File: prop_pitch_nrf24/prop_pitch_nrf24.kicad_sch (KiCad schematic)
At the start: 53 parts, among them J1 LOAD1, J2 LOAD2, J3 AVR-UPDI-6, J4 SERVO2, J5 SERVO1, Q1 MMSS8550, U1 ATtiny1616-M, U1 TPS563208DDCR, U2 HX711, U4 AZ1117-5.0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

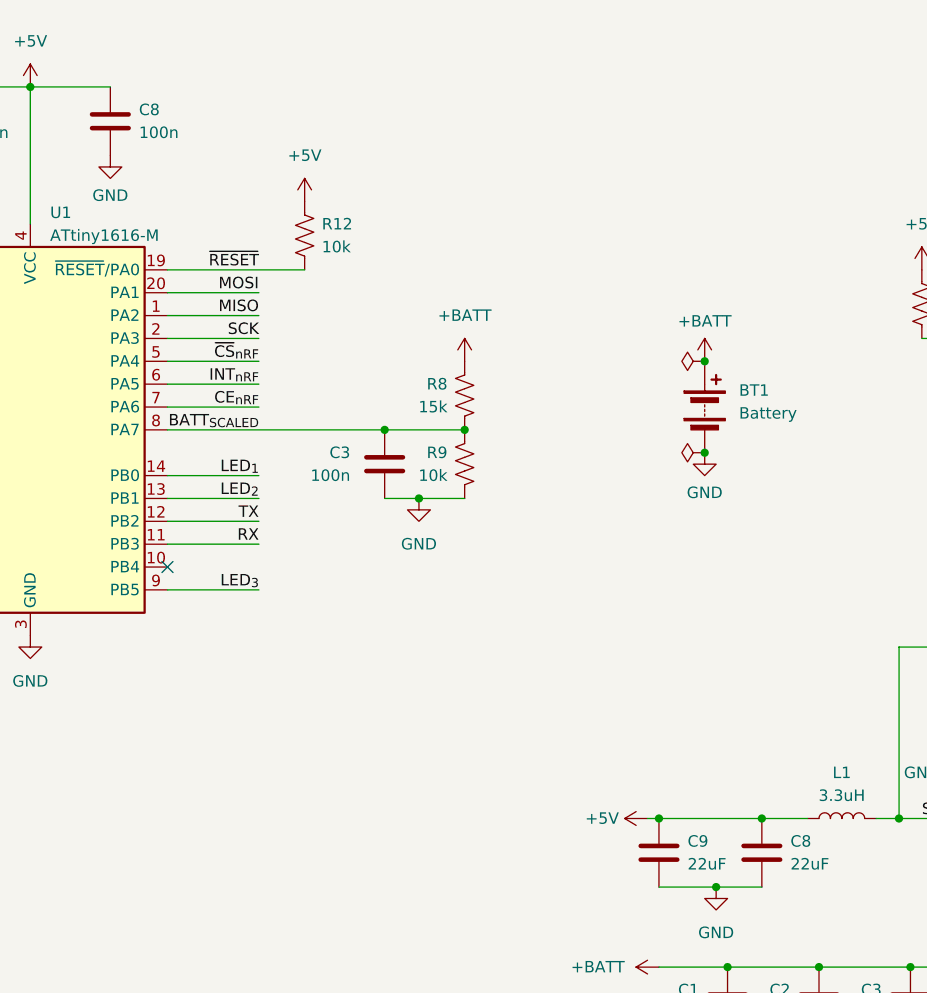
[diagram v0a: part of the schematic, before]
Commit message: Added serial header and address jumper
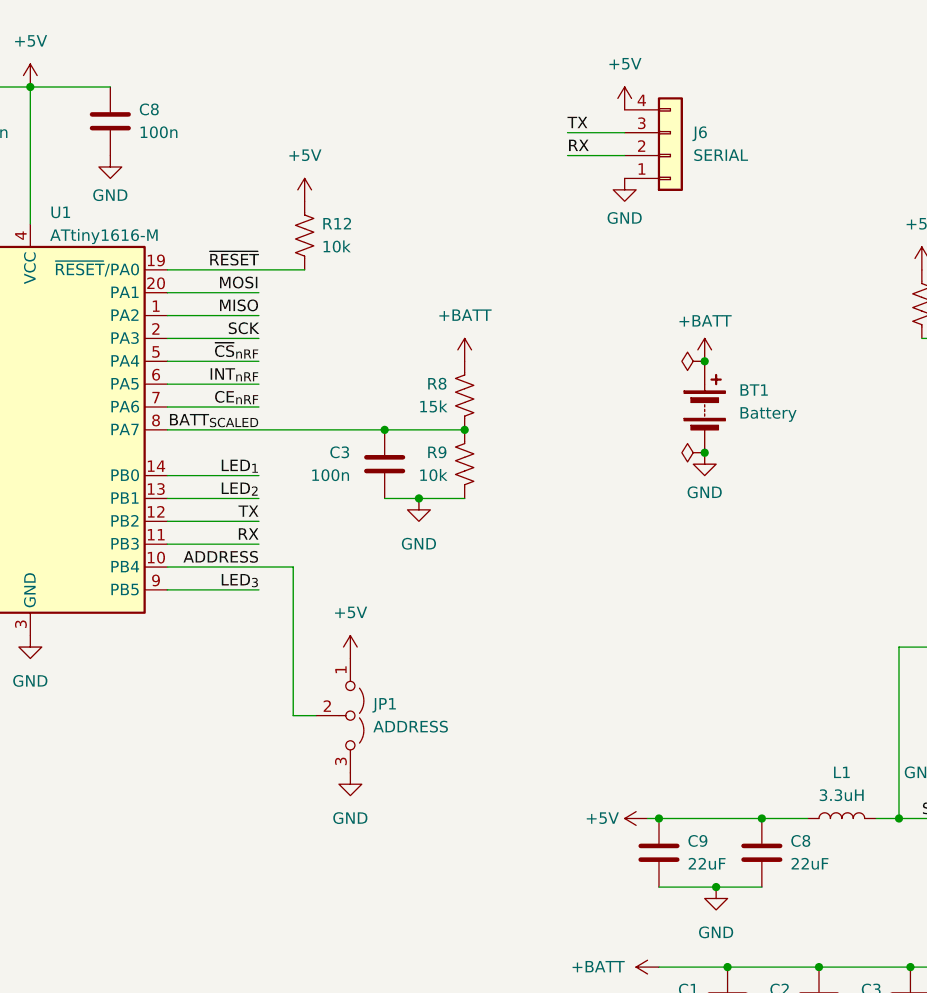
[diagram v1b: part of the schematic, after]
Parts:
- added J6: SERIAL, Connector_PinHeader_2.54mm:PinHeader_1x04_P2.54mm_Vertical, symbol Connector_Generic:Conn_01x04
- added JP1: ADDRESS, Jumper:SolderJumper-3_P1.3mm_Open_Pad1.0x1.5mm_NumberLabels, symbol Jumper:Jumper_3_Open
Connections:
- net +5V: now also J6.4 (Pin_4), JP1.1 (A)
- net GND: now also J6.1 (Pin_1), JP1.3 (B)
- net RX: now also J6.2 (Pin_2)
- net TX: now also J6.3 (Pin_3)
- net ADDRESS: now reaches U1.10 (PB4)
- net ADDRESS: now also JP1.2 (C)
- no-connect marks 2 -> 1
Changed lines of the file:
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@@
   (junction (at 229.87 171.45) (diameter 0) (color 0 0 0 0)
   )
-  (no_connect (at 121.92 76.2))
   (no_connect (at 148.59 153.67))
   (wire (pts (xy 121.92 48.26) (xy 132.08 48.26))
@@
     (stroke (width 0) (type default))
   )
+  (wire (pts (xy 121.92 76.2) (xy 135.89 76.2))
+    (stroke (width 0) (type default))
+  )
   (wire (pts (xy 133.35 133.35) (xy 135.89 133.35))
     (stroke (width 0) (type default))
@@
     (stroke (width 0) (type default))
   )
+  (wire (pts (xy 135.89 76.2) (xy 135.89 92.71))
+    (stroke (width 0) (type default))
+  )
   (wire (pts (xy 121.92 71.12) (xy 132.08 71.12))
     (stroke (width 0) (type default))
@@
     (stroke (width 0) (type default))
   )
+  (wire (pts (xy 172.72 30.48) (xy 166.37 30.48))
+    (stroke (width 0) (type default))
+  )
   (wire (pts (xy 27.94 115.57) (xy 35.56 115.57))
     (stroke (width 0) (type default))
@@
     (stroke (width 0) (type default))
   )
+  (wire (pts (xy 172.72 27.94) (xy 166.37 27.94))
+    (stroke (width 0) (type default))
+  )
   (wire (pts (xy 228.6 99.06) (xy 227.33 99.06))
     (stroke (width 0) (type default))
@@
     (stroke (width 0) (type default))
   )
+  (wire (pts (xy 135.89 92.71) (xy 138.43 92.71))
+    (stroke (width 0) (type default))
+  )
   (wire (pts (xy 40.64 162.56) (xy 50.8 162.56))
     (stroke (width 0) (type default))
@@
     (effects (font (size 1.27 1.27)) (justify left bottom))
   )
+  (label "ADDRESS" (at 132.08 76.2 180) (fields_autoplaced)
+    (effects (font (size 1.27 1.27)) (justify right bottom))
+  )
   (label "SCK" (at 214.63 48.26 0) (fields_autoplaced)
     (effects (font (size 1.27 1.27)) (justify left bottom))
@@
     (effects (font (size 1.27 1.27)) (justify right bottom))
   )
+  (label "TX" (at 166.37 27.94 0) (fields_autoplaced)
+    (effects (font (size 1.27 1.27)) (justify left bottom))
+  )
+  (label "RX" (at 166.37 30.48 0) (fields_autoplaced)
+    (effects (font (size 1.27 1.27)) (justify left bottom))
+  )
   (label "LED_{2}" (at 38.1 66.04 270) (fields_autoplaced)
     (effects (font (size 1.27 1.27)) (justify right bottom))
@@
     )
   )
+  (symbol (lib_id "power:GND") (at 172.72 33.02 0) (unit 1)
+    (in_bom yes) (on_board yes) (dnp no) (fields_autoplaced)
+    (property "Reference" "#PWR049" (at 172.72 39.37 0)
+      (effects (font (size 1.27 1.27)) hide)
+    )
+    (property "Value" "GND" (at 172.72 37.465 0)
+      (effects (font (size 1.27 1.27)))
+    )
+    (property "Footprint" "" (at 172.72 33.02 0)
+      (effects (font (size 1.27 1.27)) hide)
+    )
+    (property "Datasheet" "" (at 172.72 33.02 0)
+      (effects (font (size 1.27 1.27)) hide)
+    )
+    (pin "1")
+    (instances
+      (project "prop_pitch_nrf24"
+        (path "/a5c1c062-6aa5-4755-b14a-86c74d90c376"
+          (reference "#PWR049") (unit 1)
+        )
+      )
+    )
+  )
   (symbol (lib_id "power:+5V") (at 205.74 43.18 0) (unit 1)
     (in_bom yes) (on_board yes) (dnp no) (fields_autoplaced)
@@
     )
   )
+  (symbol (lib_id "power:+5V") (at 142.24 86.36 0) (unit 1)
+    (in_bom yes) (on_board yes) (dnp no) (fields_autoplaced)
+    (property "Reference" "#PWR048" (at 142.24 90.17 0)
+      (effects (font (size 1.27 1.27)) hide)
+    )
+    (property "Value" "+5V" (at 142.24 81.28 0)
+      (effects (font (size 1.27 1.27)))
+    )
+    (property "Footprint" "" (at 142.24 86.36 0)
+      (effects (font (size 1.27 1.27)) hide)
+    )
+    (property "Datasheet" "" (at 142.24 86.36 0)
+      (effects (font (size 1.27 1.27)) hide)
+    )
+    (pin "1")
+    (instances
+      (project "prop_pitch_nrf24"
+        (path "/a5c1c062-6aa5-4755-b14a-86c74d90c376"
+          (reference "#PWR048") (unit 1)
+        )
+      )
+    )
+  )
   (symbol (lib_id "Device:R_US") (at 104.14 147.32 0) (unit 1)
     (in_bom yes) (on_board yes) (dnp no) (fields_autoplaced)
@@
     )
   )
+  (symbol (lib_id "Jumper:Jumper_3_Open") (at 142.24 92.71 270) (unit 1)
+    (in_bom yes) (on_board yes) (dnp no) (fields_autoplaced)
+    (property "Reference" "JP1" (at 144.78 91.44 90)
+      (effects (font (size 1.27 1.27)) (justify left))
+    )
+    (property "Value" "ADDRESS" (at 144.78 93.98 90)
+      (effects (font (size 1.27 1.27)) (justify left))
+    )
+    (property "Footprint" "Jumper:SolderJumper-3_P1.3mm_Open_Pad1.0x1.5mm_NumberLabels" (at 142.24 92.71 0)
+      (effects (font (size 1.27 1.27)) hide)
+    )
+    (property "Datasheet" "~" (at 142.24 92.71 0)
+      (effects (font (size 1.27 1.27)) hide)
+    )
+    (pin "1")
+    (pin "2")
+    (pin "3")
+    (instances
+      (project "prop_pitch_nrf24"
+        (path "/a5c1c062-6aa5-4755-b14a-86c74d90c376"
+          (reference "JP1") (unit 1)
+        )
+      )
+    )
+  )
   (symbol (lib_id "power:GND") (at 40.64 170.18 0) (unit 1)
     (in_bom yes) (on_board yes) (dnp no) (fields_autoplaced)
@@
     )
   )
+  (symbol (lib_id "power:+5V") (at 172.72 25.4 0) (unit 1)
+    (in_bom yes) (on_board yes) (dnp no) (fields_autoplaced)
+    (property "Reference" "#PWR050" (at 172.72 29.21 0)
+      (effects (font (size 1.27 1.27)) hide)
+    )
+    (property "Value" "+5V" (at 172.72 20.32 0)
+      (effects (font (size 1.27 1.27)))
+    )
+    (property "Footprint" "" (at 172.72 25.4 0)
+      (effects (font (size 1.27 1.27)) hide)
+    )
+    (property "Datasheet" "" (at 172.72 25.4 0)
+      (effects (font (size 1.27 1.27)) hide)
+    )
+    (pin "1")
+    (instances
+      (project "prop_pitch_nrf24"
+        (path "/a5c1c062-6aa5-4755-b14a-86c74d90c376"
+          (reference "#PWR050") (unit 1)
+        )
+      )
+    )
+  )
   (symbol (lib_id "power:+5V") (at 148.59 163.83 270) (unit 1)
     (in_bom yes) (on_board yes) (dnp no) (fields_autoplaced)
@@
     )
   )
+  (symbol (lib_id "power:GND") (at 142.24 99.06 0) (mirror y) (unit 1)
+    (in_bom yes) (on_board yes) (dnp no) (fields_autoplaced)
+    (property "Reference" "#PWR047" (at 142.24 105.41 0)
+      (effects (font (size 1.27 1.27)) hide)
+    )
+    (property "Value" "GND" (at 142.24 104.14 0)
+      (effects (font (size 1.27 1.27)))
+    )
+    (property "Footprint" "" (at 142.24 99.06 0)
+      (effects (font (size 1.27 1.27)) hide)
+    )
+    (property "Datasheet" "" (at 142.24 99.06 0)
+      (effects (font (size 1.27 1.27)) hide)
+    )
+    (pin "1")
+    (instances
+      (project "prop_pitch_nrf24"
+        (path "/a5c1c062-6aa5-4755-b14a-86c74d90c376"
+          (reference "#PWR047") (unit 1)
+        )
+      )
+    )
+  )
   (symbol (lib_id "power:+5V") (at 135.89 133.35 0) (unit 1)
     (in_bom yes) (on_board yes) (dnp no) (fields_autoplaced)
@@
         )
       )
+    )
+  )
+  (symbol (lib_id "Connector_Generic:Conn_01x04") (at 177.8 30.48 0) (mirror x) (unit 1)
+    (in_bom no) (on_board yes) (dnp no) (fields_autoplaced)
+    (property "Reference" "J6" (at 180.34 27.94 0)
+      (effects (font (size 1.27 1.27)) (justify left))
+    )
+    (property "Value" "SERIAL" (at 180.34 30.48 0)
+      (effects (font (size 1.27 1.27)) (justify left))
+    )
+    (property "Footprint" "Connector_PinHeader_2.54mm:PinHeader_1x04_P2.54mm_Vertical" (at 177.8 30.48 0)
+      (effects (font (size 1.27 1.27)) hide)
+    )
+    (property "Datasheet" "~" (at 177.8 30.48 0)
+      (effects (font (size 1.27 1.27)) hide)
+    )
+    (pin "1")
+    (pin "2")
+    (pin "3")
+    (pin "4")
+    (instances
+      (project "prop_pitch_nrf24"
+        (path "/a5c1c062-6aa5-4755-b14a-86c74d90c376"
+          (reference "J6") (unit 1)
+        )
+      )
